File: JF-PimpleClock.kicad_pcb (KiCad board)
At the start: 2 copper layers, 190.4 x 298.6 mm, 59 parts, among them J1 Conn_01x06_Female, J2 Conn_01x08_Female, J3 Conn_01x08_Female, J4 USB_B_Micro, J5 Conn_01x01_Male, J6 Conn_01x01_Male, J7 Conn_01x01_Male, J8 Conn_01x01_Male, Q1 Q_PMOS_DSG, SW1 SW_Push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

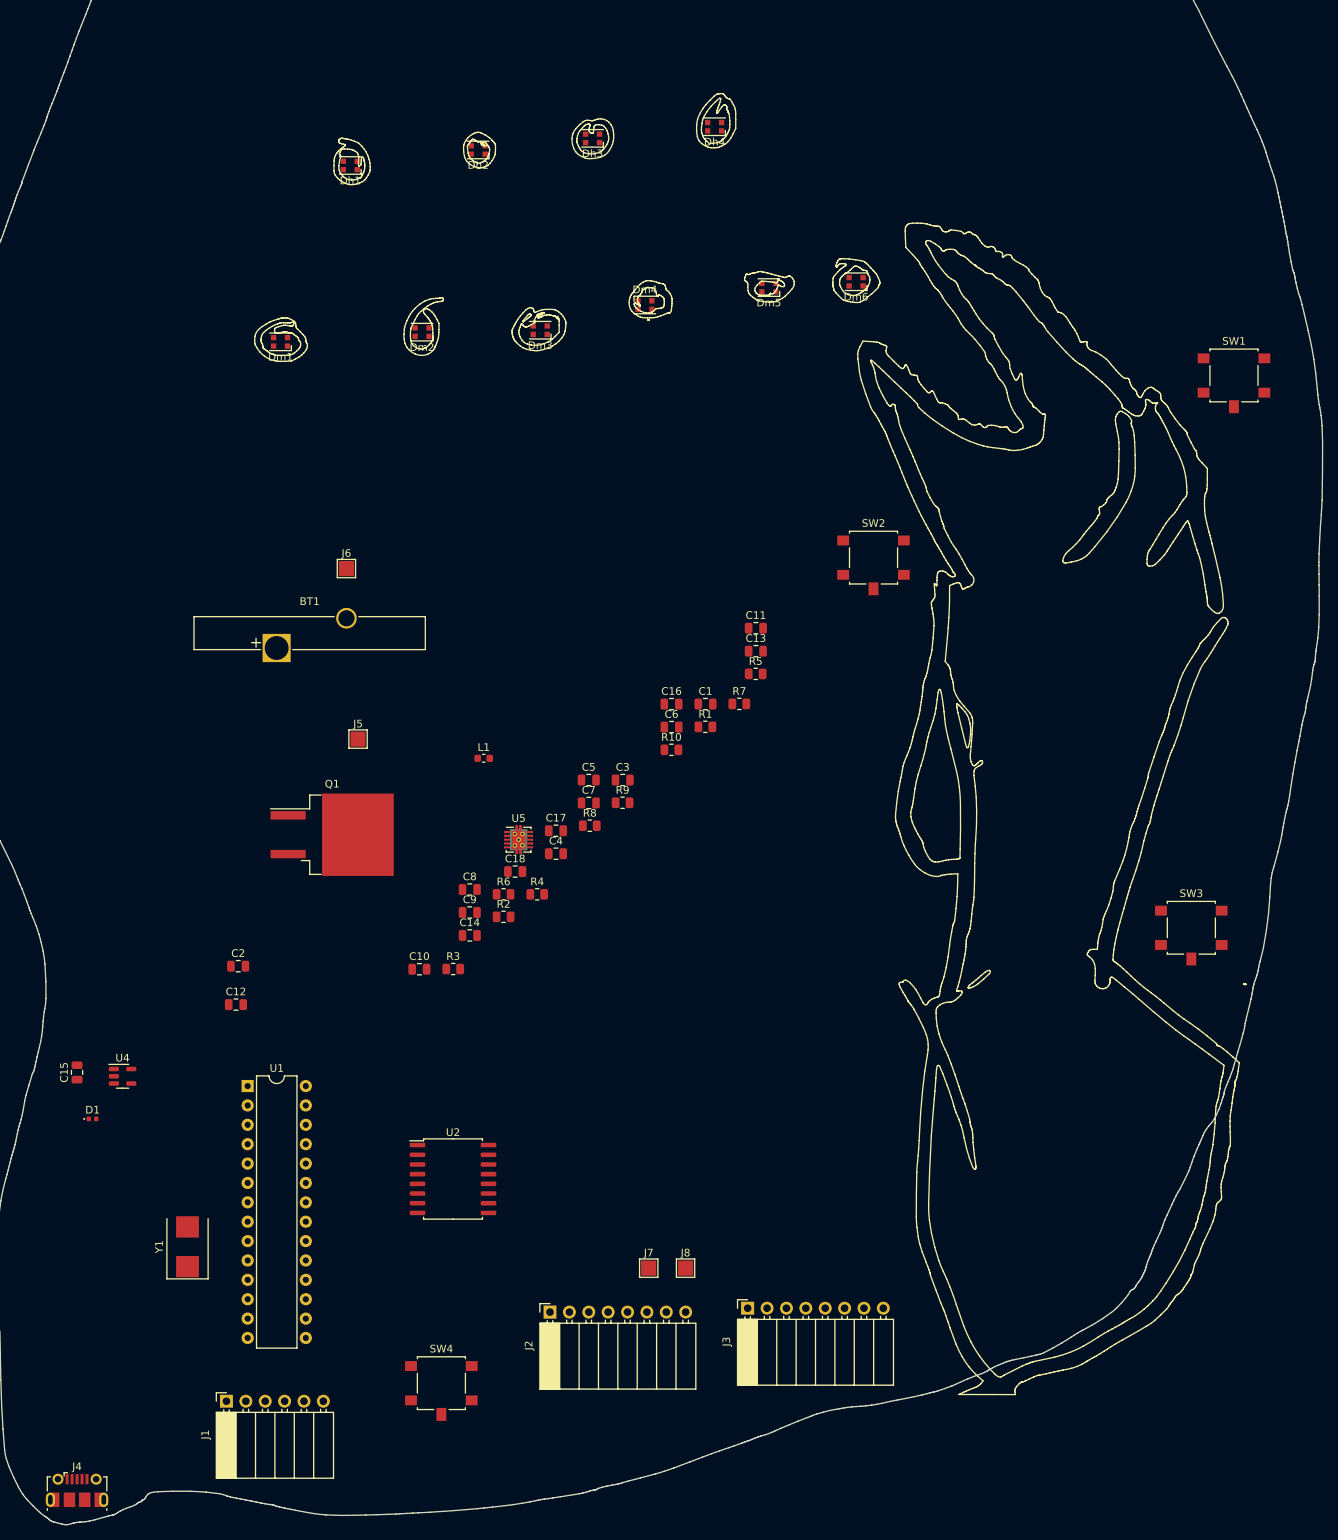
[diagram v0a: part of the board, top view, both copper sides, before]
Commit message: started first pcb test layout and some part assignment to jcl
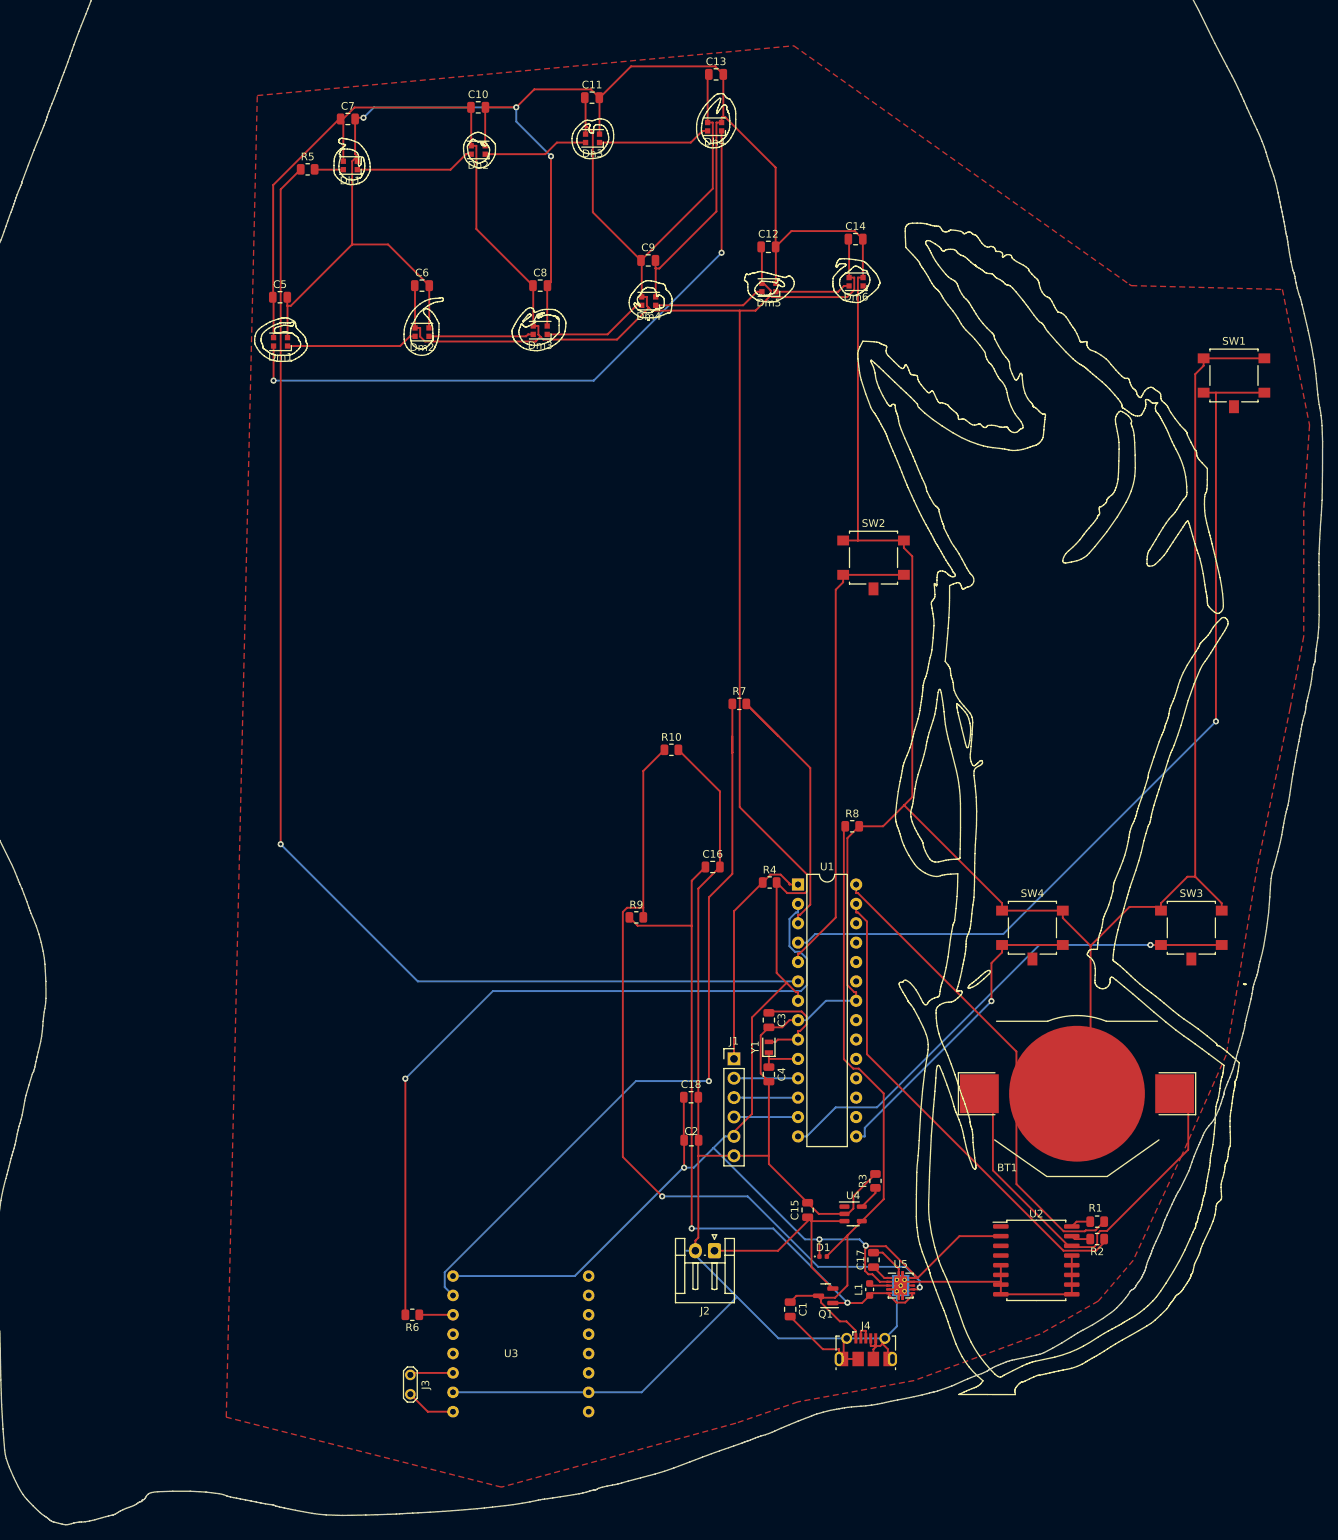
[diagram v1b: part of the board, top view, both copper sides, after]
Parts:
- removed J5, J6, J7, J8: Conn_01x01_Male, TestPoint:TestPoint_Pad_2.0x2.0mm
- added U3: DFR0299, Arduino_Nano:DFPlayer_V2, F.Cu at (84.1, -32.7)
- BT1: footprint Battery:Battery_Panasonic_CR3032-VCN_Vertical_CircularHoles -> Battery:BatteryHolder_Keystone_3002_1x2032
- J1: footprint Connector_PinSocket_2.54mm:PinSocket_1x06_P2.54mm_Horizontal -> Connector_PinHeader_2.54mm:PinHeader_1x06_P2.54mm_Vertical
- J2: value Conn_01x08_Female -> Conn_01x02; footprint Connector_PinSocket_2.54mm:PinSocket_1x08_P2.54mm_Horizontal -> Connector_JST:JST_EH_S2B-EH_1x02_P2.50mm_Horizontal
- J3: value Conn_01x08_Female -> Conn_01x02; footprint Connector_PinSocket_2.54mm:PinSocket_1x08_P2.54mm_Horizontal -> TestPoint:TestPoint_2Pads_Pitch2.54mm_Drill0.8mm
- Q1: footprint Package_TO_SOT_SMD:TO-263-2 -> Package_TO_SOT_SMD:SOT-23
- Y1: footprint Crystal:Crystal_SMD_7050-2Pin_7.0x5.0mm -> Crystal:Crystal_SMD_2012-2Pin_2.0x1.2mm
- moved C12 121.4 mm to (117.8, -167.6)
- moved BT1 120.1 mm to (158.2, -56.6)
- moved C10 113.2 mm to (79.8, -185.9)
- moved J4 105.0 mm to (130.6, -23.1)
- moved C14 104.3 mm to (129.2, -168.7)
- moved SW4 97.8 mm to (152.4, -77.5)
- moved C15 97.4 mm to (122.9, -41.4)
- moved D1 97.4 mm to (125.0, -35.3)
- moved U4 97.4 mm to (128.9, -40.9)
- moved C7 95.1 mm to (62.7, -184.4)
- moved C9 88.6 mm to (102.0, -165.9)
- moved R2 88.5 mm to (160.9, -37.6), turned to 180 degrees
- moved Q1 88.5 mm to (125.3, -30.2), turned to 180 degrees
- moved R5 88.4 mm to (57.4, -177.8)
- moved L1 86.1 mm to (131.1, -31.0), turned to 90 degrees
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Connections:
- J2 pad 1: /5v -> Net-(BT2-Pad1)
- J2 pad 2: Net-(J2-Pad2) -> GND
- J3 pad 1: unconnected-(J3-Pad1) -> Net-(LS1-Pad1)
- J3 pad 2: GND -> Net-(LS1-Pad2)
- R6 pad 1: Net-(J2-Pad2) -> Net-(R6-Pad1)
- R6 pad 2: /MCU_TX -> /MCU_RX
- R7 pad 1: Net-(J2-Pad3) -> Net-(R7-Pad1)
- R7 pad 2: /MCU_RX -> /MCU_TX
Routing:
- net GND: track 0.00 -> 771.9 mm, vias 0 -> 3
- net /5v: track 0.00 -> 469.6 mm, vias 0 -> 3
- net /NeoPixel_D: track 0.00 -> 164.8 mm, vias 0 -> 1
- net /SW1: track 0.00 -> 117.8 mm, vias 0 -> 1
- net Net-(R10-Pad1): track 0.00 -> 105.8 mm, vias 0 -> 2
- net Net-(R7-Pad1): track 0.00 -> 101.3 mm, vias 0 -> 1
- net /MCU_RX: track 0.00 -> 101.3 mm, vias 0 -> 1
- net Net-(C16-Pad1): track 0.00 -> 94.1 mm, vias 0 -> 2
- net Net-(Dh4-Pad1): track 0.00 -> 86.2 mm, vias 0 -> 2
- net Net-(C1-Pad1): track 0.00 -> 85.4 mm
- net /SW3: track 0.00 -> 65.9 mm, vias 0 -> 1
- net /SDA: track 0.00 -> 63.1 mm
- net /SCL: track 0.00 -> 62.7 mm
- net /SW2: track 0.00 -> 61.3 mm
- net Net-(BT1-Pad1): track 0.00 -> 50.6 mm
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- added copper zone on F.Cu, net GND

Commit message: update pcb layout, swapped a few parts to make them easier for assembly
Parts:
- BT1: footprint Battery:BatteryHolder_Keystone_3002_1x2032 -> Battery:BatteryHolder_Keystone_1060_1x2032
- Y1: footprint Crystal:Crystal_SMD_2012-2Pin_2.0x1.2mm -> Crystal:Crystal_SMD_HC49-SD
- moved R7 86.6 mm to (71.1, -32.5), turned to 180 degrees
- moved R10 66.8 mm to (135.1, -42.1), turned to 90 degrees
- moved R8 55.2 mm to (115.4, -38.1)
- moved R9 54.8 mm to (135.1, -37.3)
- moved C16 50.9 mm to (130.6, -39.6), turned to 180 degrees
- moved R3 24.5 mm to (111.9, -31.0), turned to 180 degrees
- moved U4 15.5 mm to (115.8, -32.5), turned to 180 degrees
- moved J2 13.2 mm to (111.8, -22.9)
- moved D1 10.7 mm to (124.5, -24.6)
- moved C15 9.77 mm to (120.3, -32.0), turned to -90 degrees
- moved C18 6.58 mm to (109.2, -49.8)
- moved J1 6.51 mm to (117.3, -56.1)
- moved C3 6.28 mm to (111.8, -67.8)
- moved C4 6.24 mm to (111.8, -60.5), turned to 90 degrees
- moved C2 5.79 mm to (109.2, -45.0)
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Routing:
- net GND: track 771.9 -> 94.6 mm, vias 3 -> 41
- net /5v: track 469.6 -> 299.5 mm, vias 3 -> 0
- net Net-(R7-Pad1): track 101.3 -> 5.38 mm, vias 1 -> 0
- net Net-(R10-Pad1): track 105.8 -> 12.9 mm
- net Net-(C16-Pad1): track 94.1 -> 42.6 mm, vias 2 -> 4
- net Net-(C1-Pad1): track 85.4 -> 34.7 mm
- net /MCU_TX: track 39.0 -> 70.7 mm
- net /SW3: track 65.9 -> 97.5 mm, vias 1 -> 0
- net /NeoPixel_D: track 164.8 -> 134.5 mm
- net /SW4: track 41.6 -> 66.9 mm, vias 1 -> 0
- net Net-(BT1-Pad1): track 50.6 -> 26.0 mm
- net /MCU_RX: track 101.3 -> 78.3 mm, vias 1 -> 0
- net Net-(Dh4-Pad1): track 86.2 -> 96.4 mm, vias 2 -> 0
- net Net-(C3-Pad1): track 12.9 -> 19.9 mm
- net /SDA: track 63.1 -> 57.5 mm
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- added copper zone on F.Cu, net /5v
- added copper zone on B.Cu, net GND
- removed copper zone on F.Cu, net GND

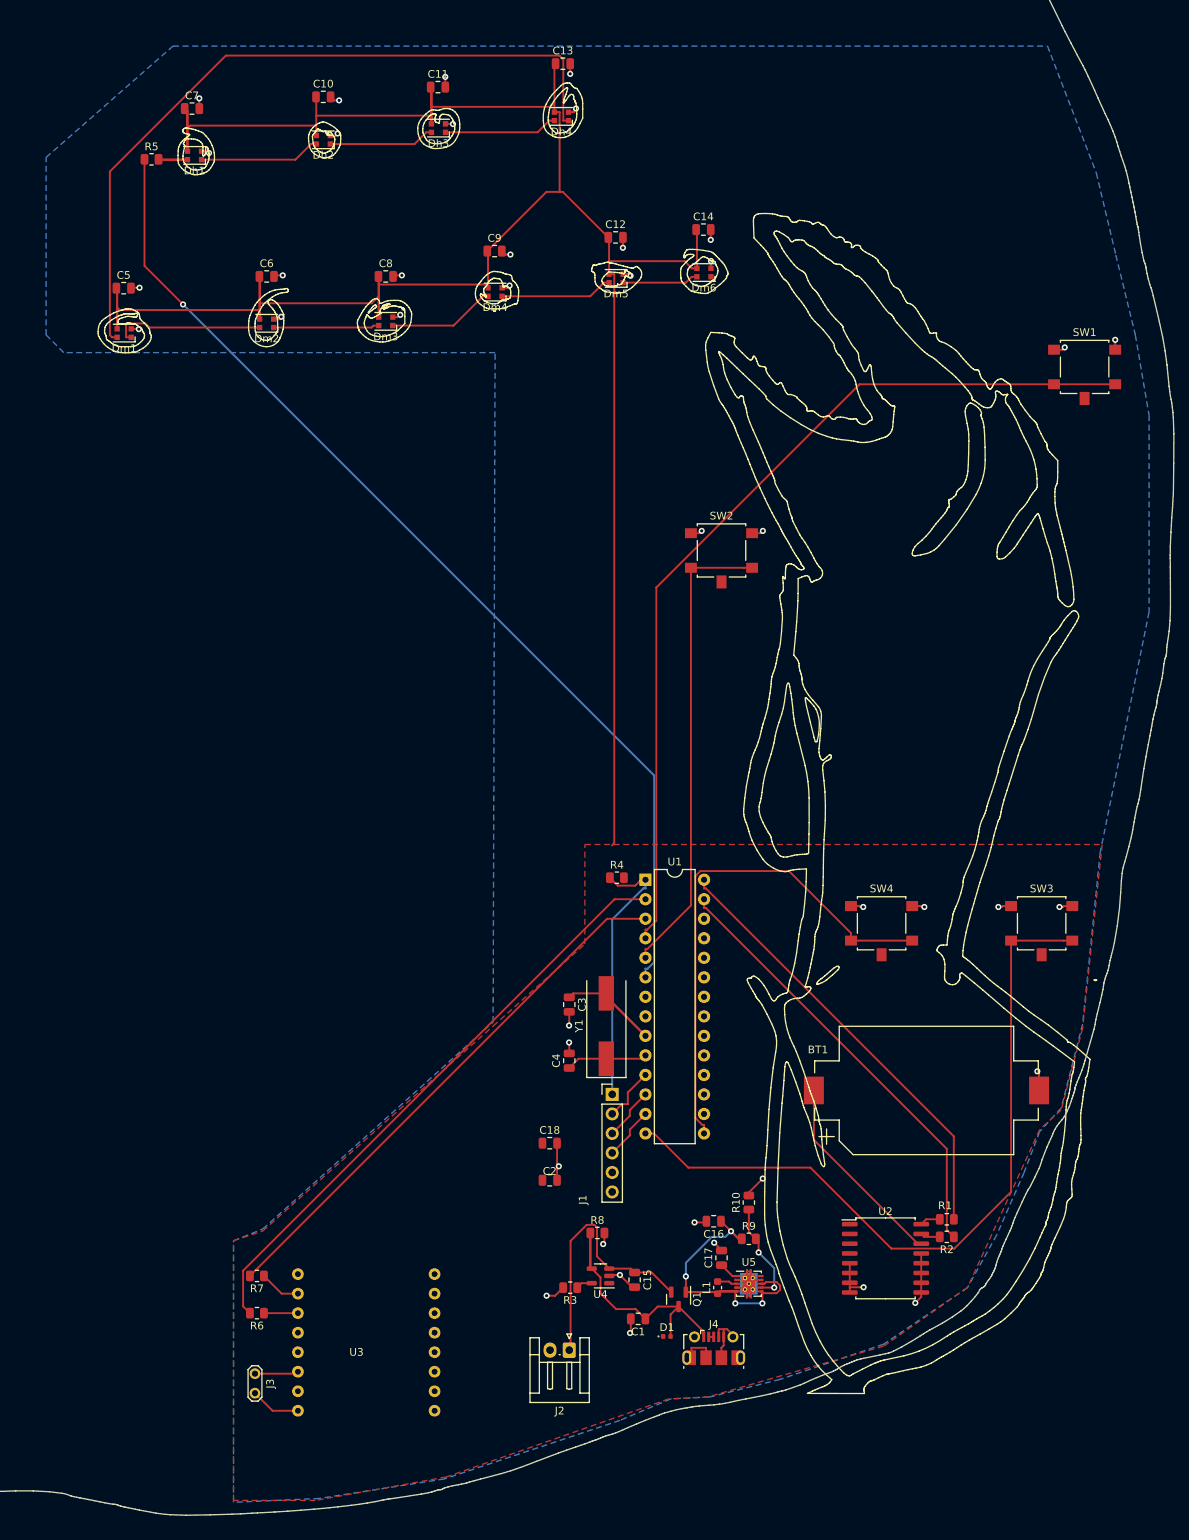
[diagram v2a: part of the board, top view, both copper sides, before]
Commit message: revisions for pcb layout, new cheaper parts selected, this went out into a test production
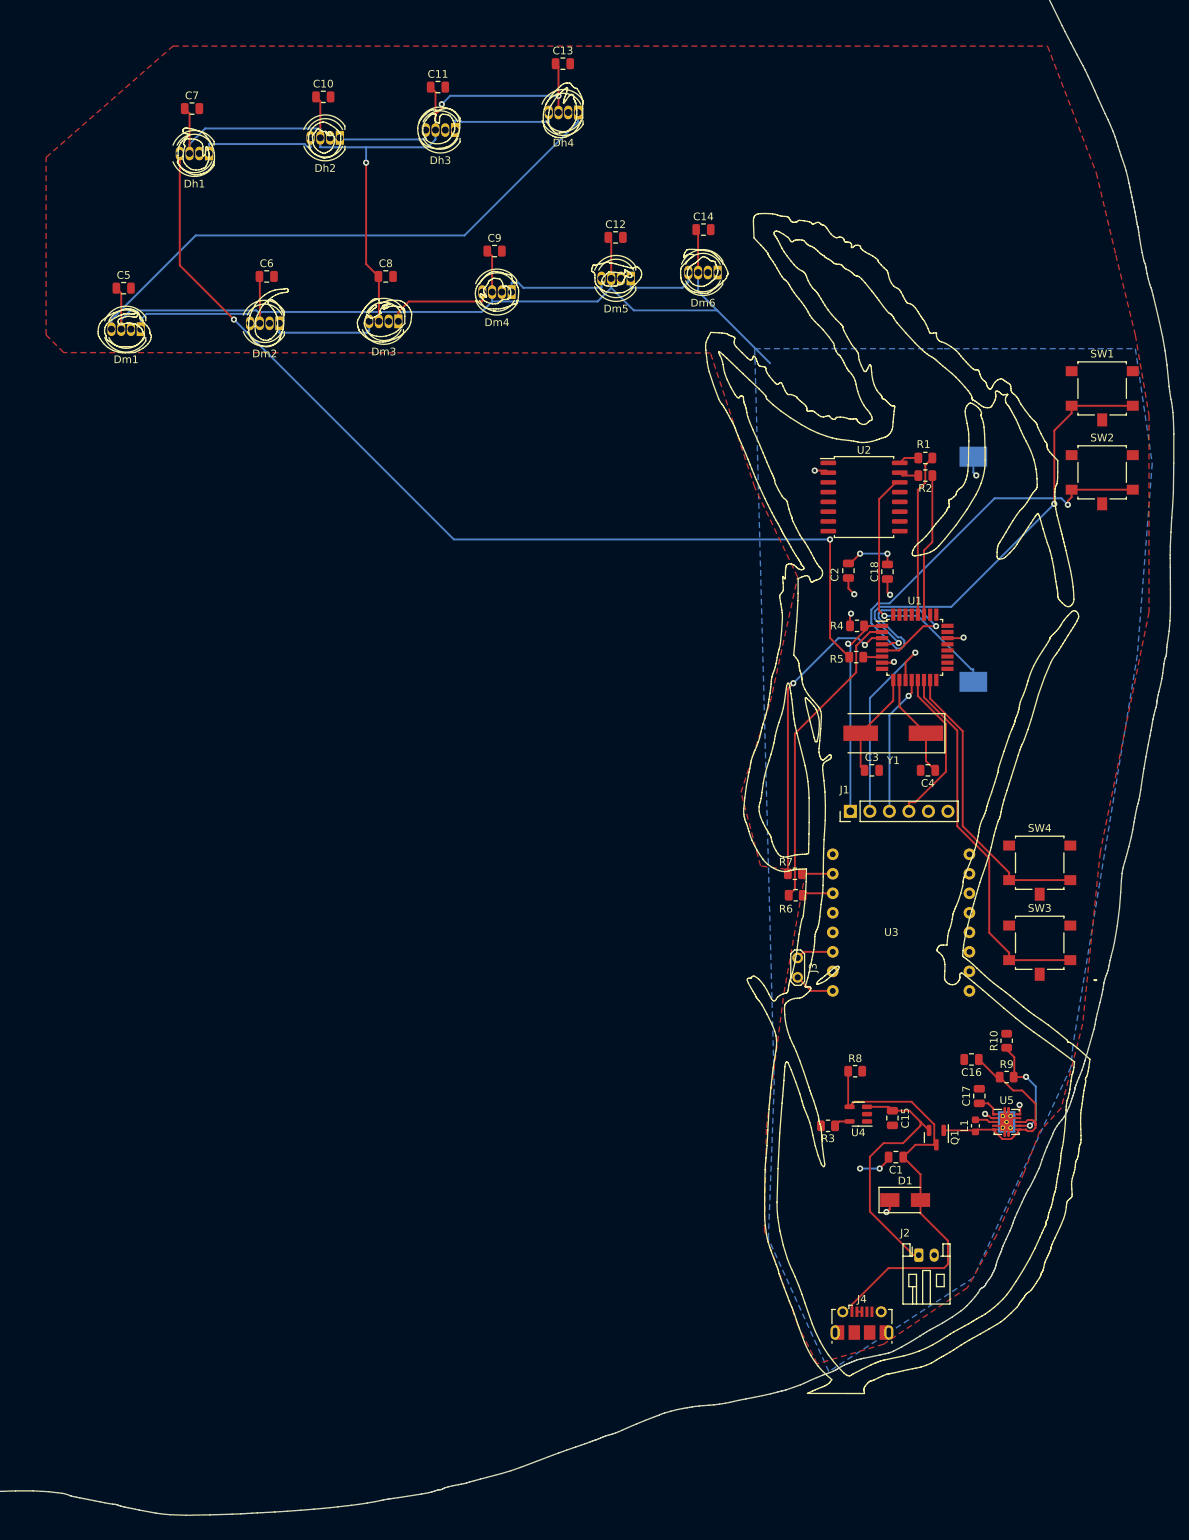
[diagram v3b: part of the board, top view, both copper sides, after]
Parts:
- BT1: moved to B.Cu
- D1: footprint Diode_SMD:D_0402_1005Metric -> Diode_SMD:D_SMA
- Dh1, Dh2, Dh3, Dh4, Dm1, Dm2, Dm3, Dm4, Dm5, Dm6: footprint LED_SMD:LED_WS2812B-2020_PLCC4_2.0x2.0mm -> LED_THT:LED_D5.0mm-4_RGB
- J2: footprint Connector_JST:JST_EH_S2B-EH_1x02_P2.50mm_Horizontal -> Connector_JST:JST_PH_S2B-PH-K_1x02_P2.00mm_Horizontal
- U1: footprint Package_DIP:DIP-28_W7.62mm -> Package_QFP:TQFP-32_7x7mm_P0.8mm
- moved R5 112.3 mm to (149.1, -113.0), turned to 180 degrees
- moved R1 99.1 mm to (158.1, -138.9)
- moved R2 99.1 mm to (158.1, -136.7)
- moved U2 99.1 mm to (150.1, -133.9)
- moved J3 89.0 mm to (141.5, -73.9)
- moved R6 88.7 mm to (141.2, -82.0)
- moved U3 88.5 mm to (153.7, -87.4)
- moved C2 88.3 mm to (148.1, -124.3), turned to 90 degrees
- moved R7 87.4 mm to (141.1, -84.8)
- moved C18 86.4 mm to (153.2, -124.1), turned to 90 degrees
- moved BT1 68.1 mm to (164.3, -124.5), turned to 90 degrees
- moved C4 60.0 mm to (158.4, -98.3), turned to 180 degrees
- moved Y1 53.3 mm to (153.9, -103.1), turned to 180 degrees
- moved SW2 50.6 mm to (181.1, -136.1)
- moved C3 49.8 mm to (151.1, -98.3), turned to 0 degrees
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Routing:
- net /NeoPixel_D: track 134.5 -> 2.49 mm, vias 1 -> 0
- net Net-(Dh1-Pad4): track 7.50 -> 130.3 mm, vias 0 -> 2
- net GND: track 94.6 -> 18.4 mm, vias 41 -> 6
- net /SW1: track 117.0 -> 58.4 mm, vias 0 -> 2
- net /5v: track 299.5 -> 248.6 mm, vias 0 -> 11
- net /SW3: track 97.5 -> 49.0 mm
- net /SDA: track 57.5 -> 18.6 mm
- net /MCU_RX: track 78.3 -> 40.2 mm
- net /SCL: track 57.8 -> 21.2 mm
- net /MCU_TX: track 70.7 -> 39.8 mm, vias 0 -> 2
- net /SW4: track 66.9 -> 38.3 mm
- net Net-(Dh4-Pad1): track 96.4 -> 73.8 mm
- net Net-(C1-Pad1): track 34.7 -> 57.2 mm
- net /MOSI: track 7.30 -> 27.2 mm, vias 0 -> 1
- net /SCK: track 6.85 -> 21.1 mm
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- added copper zone on B.Cu, net /5v
- added copper zone on F.Cu, net GND
- removed copper zone on F.Cu, net /5v
- removed copper zone on B.Cu, net GND
